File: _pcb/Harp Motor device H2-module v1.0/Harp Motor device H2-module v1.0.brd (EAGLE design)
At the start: 47.1 x 57.9 mm, 45 parts, among them IC1 FT232RL, IC3 LP5907MFX-3.3, IC7 USBLC6-2SC6, IC8 ATXMEGA32A4U, X15 Main_plug, X3 USB_MINI_B

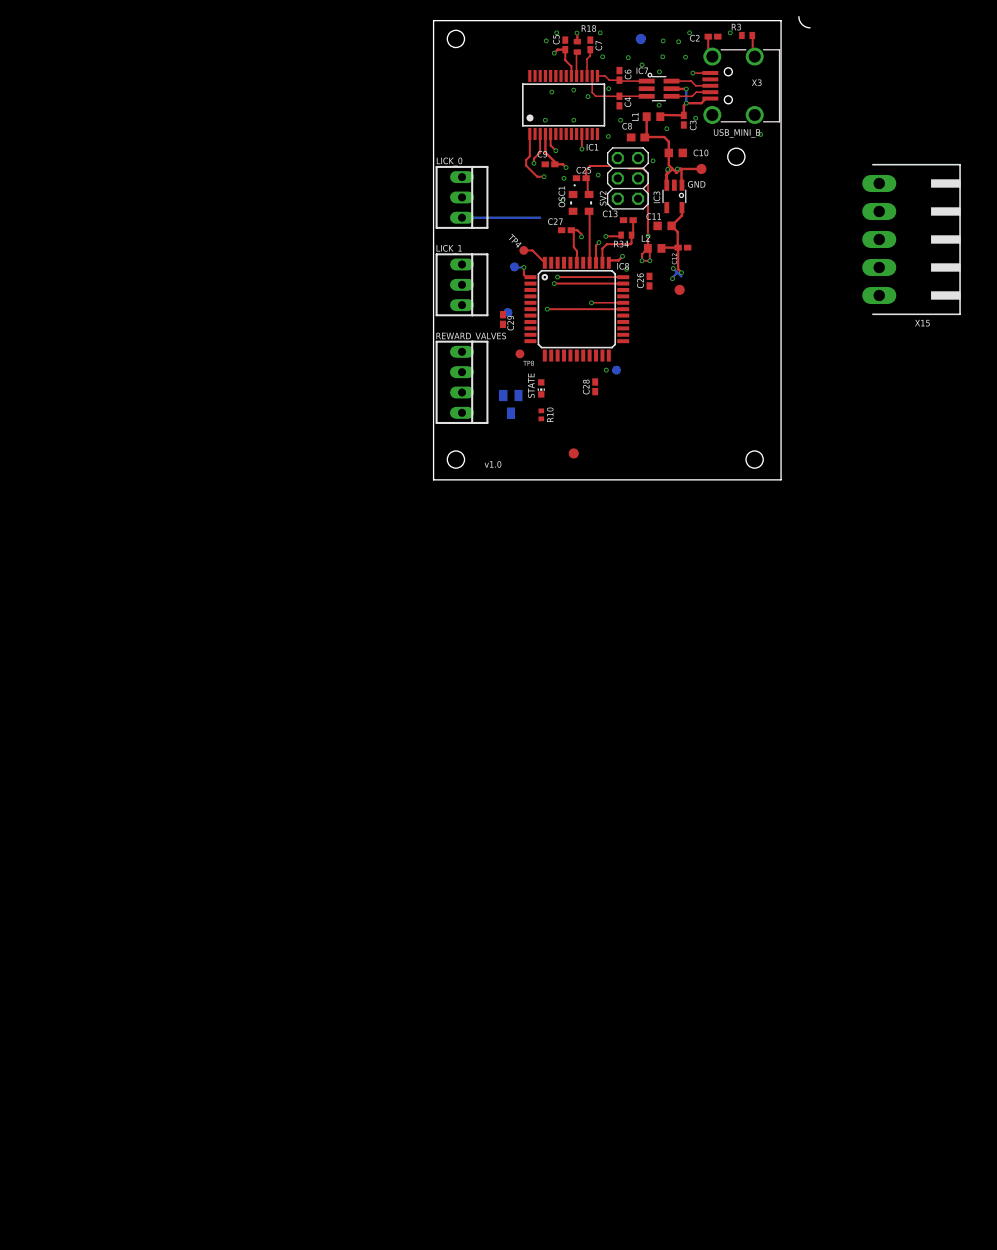
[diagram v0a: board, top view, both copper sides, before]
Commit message: Harp Motor device H2 - design
still first steps on Eagle Harp Motor device H2 design
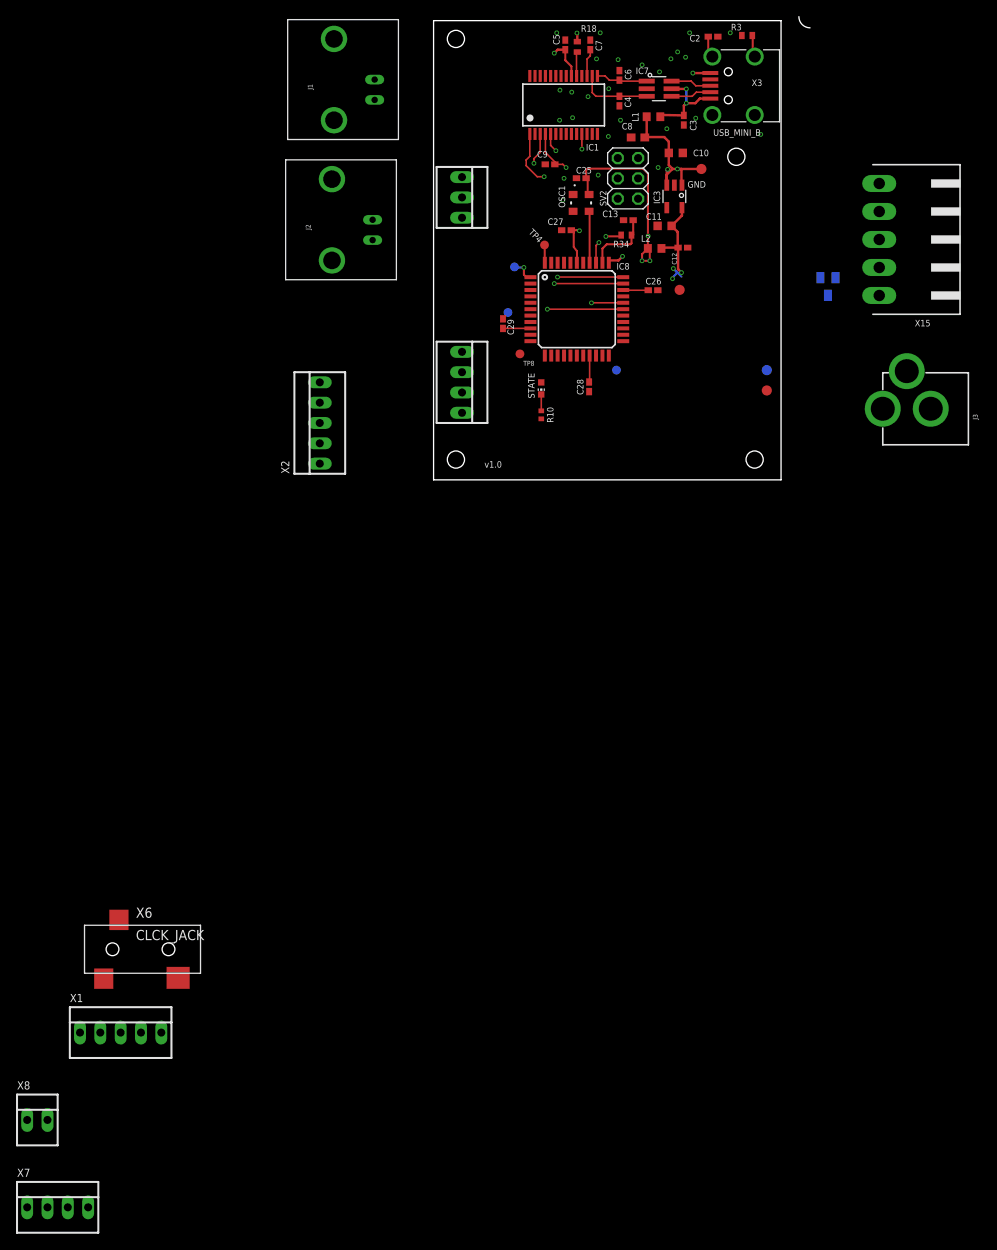
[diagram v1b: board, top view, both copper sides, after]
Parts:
- removed LICK_1: 1x3 case, con-molex:22-23-2031
- added J1, J2: BNCPTH, SparkFun-Connectors:BNC
- added J3: POWER_JACK, SparkFun-Connectors:POWER_JACK_PTH
- added X1, X2: 22-23-2051, con-molex:22-23-2051
- added X6: CLCK_JACK, harp input expander:35RASMT2BHNTRX
- added X7: 1x4 case, con-molex:22-23-2041
- added X8: 22-23-2021, con-molex:22-23-2021
- moved TP11 44.3 mm to (41.7, 13.7)
- moved D4 42.3 mm to (49.3, 24.2)
- moved TP10 25.4 mm to (41.7, 11.2)
- moved TP4 2.68 mm to (13.9, 29.4)
- moved C26 1.22 mm to (27.4, 23.7), turned to 0 degrees
- moved C28 0.76 mm to (19.4, 11.6)
- moved C29 0.51 mm to (8.68, 19.5)
- renumbered LICK_0 to X5, REWARD_VALVES to X4
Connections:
- removed net HARP_H1_BOARD_RX: X15.3
- removed net HARP_H1_BOARD_TX: X15.2
- new net HARP_H1_RX: X1.3
- new net HARP_H1_TX: X1.4
- new net N$4: X1.5, X2.5, X4.4
- net +3V3: no longer LICK_1.3
- net GND: now also X1.1, X2.1, X4.1, X6.5; no longer LICK_1.1
- net HARP_H1_CLOCK_IN: now also X1.2; no longer X15.4
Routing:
- net +5V: track 91.5 -> 55.3 mm, vias 6 -> 4
- net +3V3: track 95.2 -> 63.9 mm, vias 7 -> 6
- net +3V3_U: track 41.6 -> 53.5 mm
- net HARP_H1_BOARD_RX: track 6.17 -> 0.00 mm, vias 1 -> 0
- net N$9: track 0.00 -> 2.05 mm
- net N$11: track 3.27 -> 2.24 mm
